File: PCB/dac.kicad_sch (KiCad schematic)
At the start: 29 parts, among them U1 ES9038Q2M, Y1 ASE-50MHz

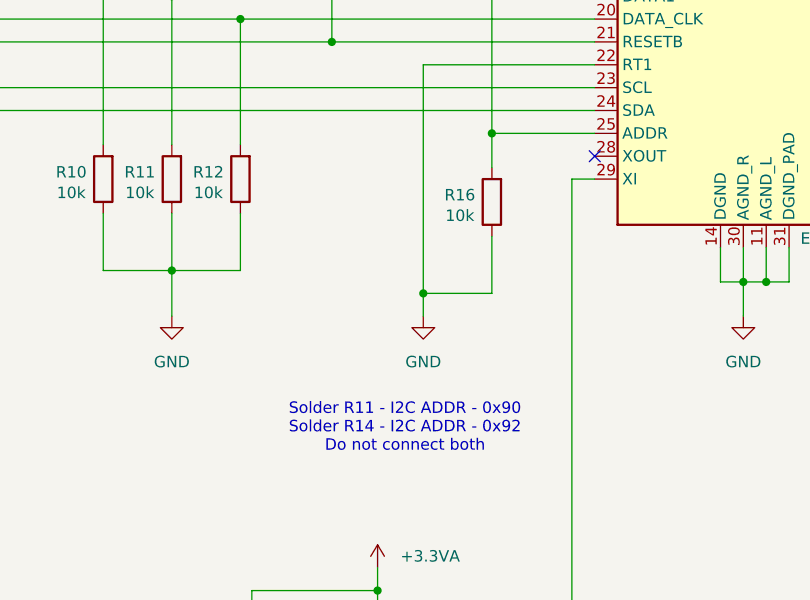
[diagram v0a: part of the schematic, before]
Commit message: Routing revised, added some missing parameters to components
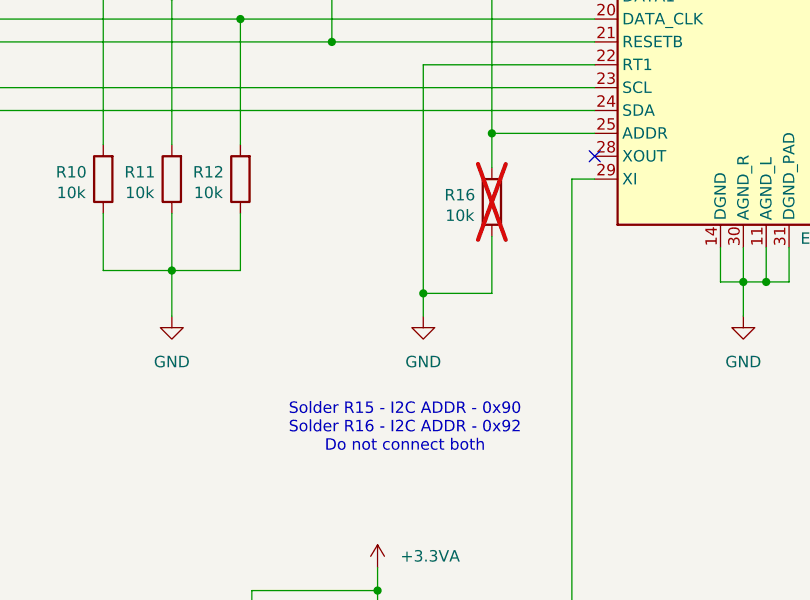
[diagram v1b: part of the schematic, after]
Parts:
- C3, C4, C5, C6, C7, C8: Voltage 6.3V -> 16V
- R16: now not fitted
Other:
- note added: "Solder R15 - I2C ADDR - 0x90 Solder R16 - I2C ADDR - 0x92 Do not connect both"
- note removed: "Solder R11 - I2C ADDR - 0x90 Solder R14 - I2C ADDR - 0x92 Do not connect both"
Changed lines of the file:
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@@
 		)
 	)
-	(text "Solder R11 - I2C ADDR - 0x90\nSolder R14 - I2C ADDR - 0x92\nDo not connect both"
+	(text "Solder R15 - I2C ADDR - 0x90\nSolder R16 - I2C ADDR - 0x92\nDo not connect both"
 		(exclude_from_sim no)
 		(at 135.128 136.906 0)
@@
 			)
 		)
-		(property "Voltage" "6.3V"
+		(property "Voltage" "16V"
 			(at 209.55 33.02 0)
 			(effects
@@
 			)
 		)
-		(property "Voltage" "6.3V"
+		(property "Voltage" "16V"
 			(at 163.83 52.07 0)
 			(effects
@@
 			)
 		)
-		(property "Voltage" "6.3V"
+		(property "Voltage" "16V"
 			(at 220.98 33.02 0)
 			(effects
@@
 		(in_bom yes)
 		(on_board yes)
-		(dnp no)
+		(dnp yes)
 		(property "Reference" "R16"
 			(at 141.224 110.998 0)
@@
 			)
 		)
-		(property "Voltage" "6.3V"
+		(property "Voltage" "16V"
 			(at 243.84 33.02 0)
 			(effects
@@
 			)
 		)
-		(property "Voltage" "6.3V"
+		(property "Voltage" "16V"
 			(at 232.41 33.02 0)
 			(effects
@@
 			)
 		)
-		(property "Voltage" "6.3V"
+		(property "Voltage" "16V"
 			(at 243.84 55.88 0)
 			(effects

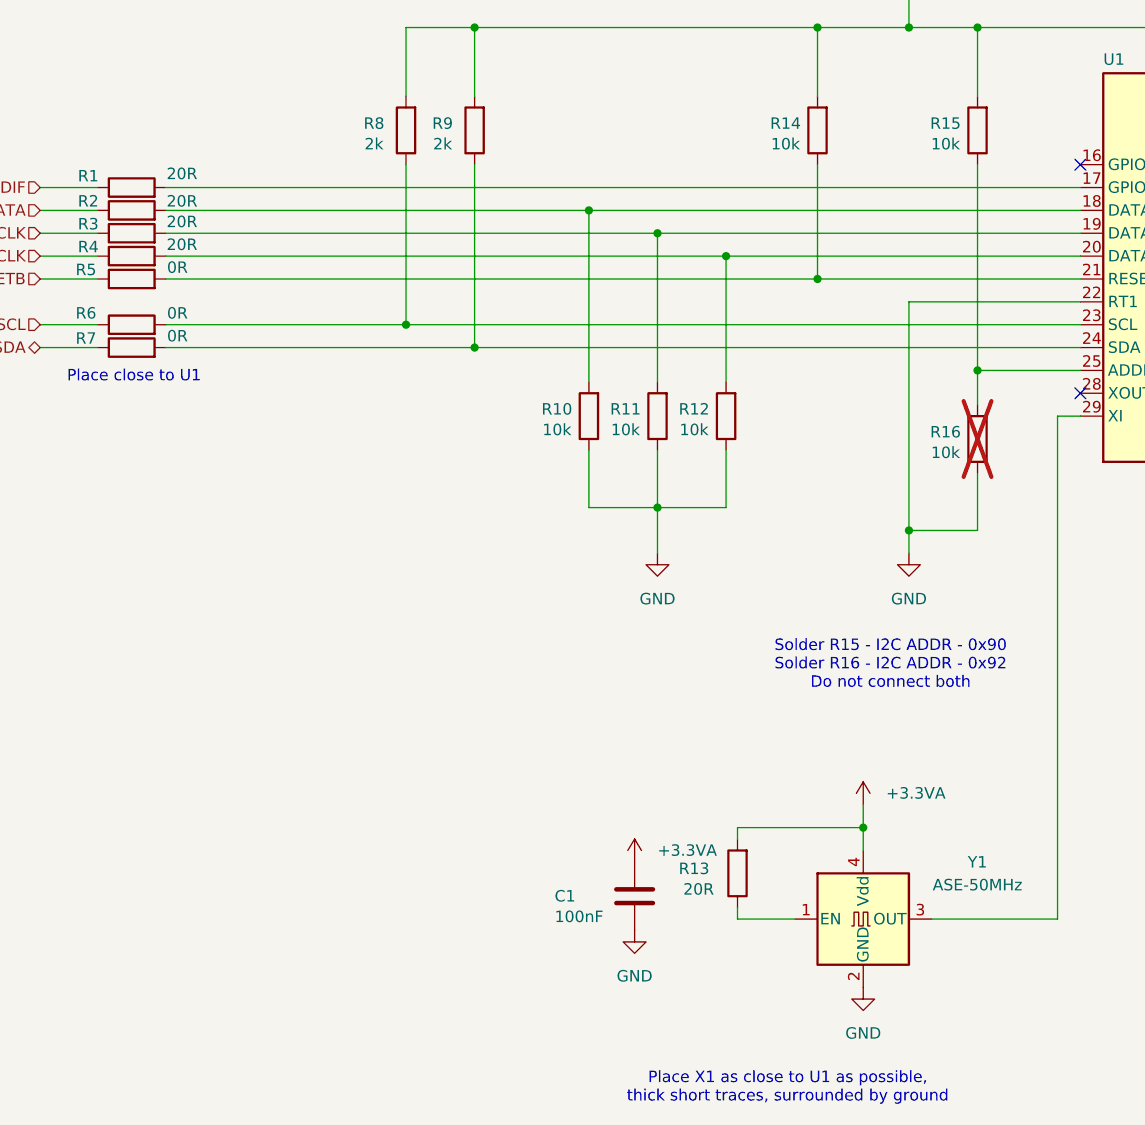
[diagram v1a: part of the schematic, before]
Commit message: Updated PCB with digital traxce suggestions. Added JLCPCB Pns
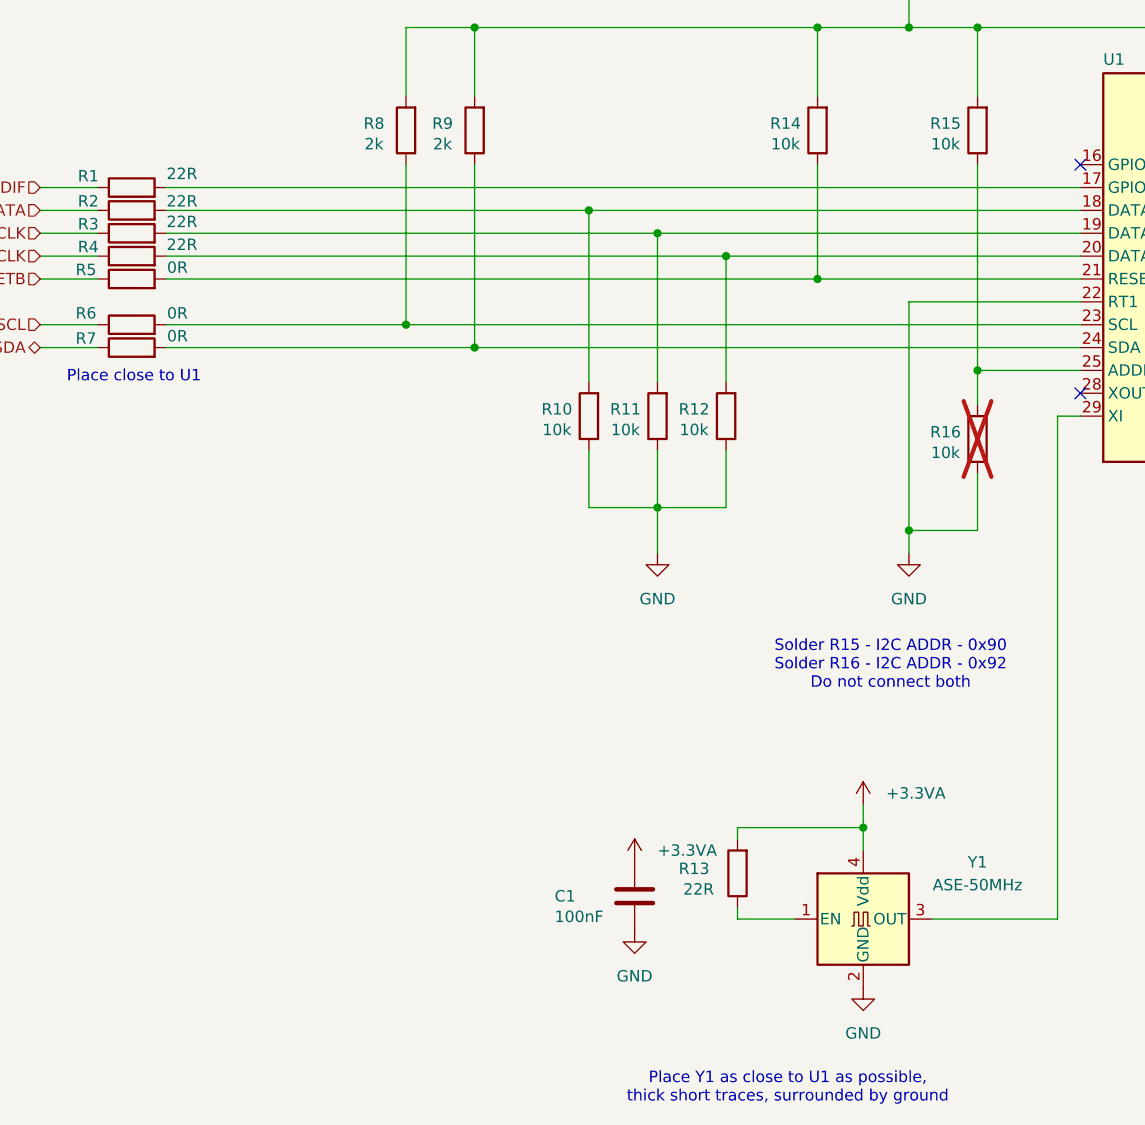
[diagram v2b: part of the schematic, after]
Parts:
- C1: JLCPCBPn (none) -> C1525; Voltage 25V -> 16V
- C3, C4, C5, C6, C7, C8: JLCPCBPn (none) -> C15849
- R1, R13, R2, R3, R4: value 20R -> 22R; JLCPCBPn (none) -> C25092
- R10, R11, R12, R14, R15: JLCPCBPn (none) -> C25744
- R17, R18, R19, R20, R5, R6, R7: JLCPCBPn (none) -> C17168
- R8, R9: JLCPCBPn (none) -> C4109
- U1: JLCPCBPn (none) -> C2682306
- Y1: JLCPCBPn (none) -> C19725350
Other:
- note added: "Place Y1 as close to U1 as possible, thick short traces, surrounded by ground"
- note removed: "Place X1 as close to U1 as possible, thick short traces, surrounded by ground"

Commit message: Added filter capacitors to OPA1622 circuitry
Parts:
- C1: JLCPCBPn C1525 -> (none); LCSC Part # (none) -> C1525
- C3, C4, C5, C6, C7, C8: JLCPCBPn C15849 -> (none); LCSC Part # (none) -> C15849
- R1, R13, R2, R3, R4: JLCPCBPn C25092 -> (none); LCSC Part # (none) -> C25092
- R10, R11, R12, R14, R15: JLCPCBPn C25744 -> (none); LCSC Part # (none) -> C25744
- R17, R18, R19, R20, R5, R6, R7: JLCPCBPn C17168 -> (none); LCSC Part # (none) -> C17168
- R8, R9: JLCPCBPn C4109 -> (none); LCSC Part # (none) -> C4109
- U1: JLCPCBPn C2682306 -> (none); LCSC Part # (none) -> C2682306
- Y1: JLCPCBPn C19725350 -> (none); LCSC Part # (none) -> C19725350
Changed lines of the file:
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@@
 			)
 		)
-		(property "JLCPCBPn" "C4109"
+		(property "LCSC Part #" "C4109"
 			(at 88.9 77.47 0)
 			(effects
@@
 			)
 		)
-		(property "JLCPCBPn" "C15849"
+		(property "LCSC Part #" "C15849"
 			(at 209.55 33.02 0)
 			(effects
@@
 			)
 		)
-		(property "JLCPCBPn" "C25092"
+		(property "LCSC Part #" "C25092"
 			(at 50.8 88.9 0)
 			(effects
@@
 			)
 		)
-		(property "JLCPCBPn" "C1525"
+		(property "LCSC Part #" "C1525"
 			(at 106.68 162.56 0)
 			(effects
@@
 			)
 		)
-		(property "JLCPCBPn" "C15849"
+		(property "LCSC Part #" "C15849"
 			(at 163.83 52.07 0)
 			(effects
@@
 			)
 		)
-		(property "JLCPCBPn" "C15849"
+		(property "LCSC Part #" "C15849"
 			(at 220.98 33.02 0)
 			(effects
@@
 			)
 		)
-		(property "JLCPCBPn" "C25092"
+		(property "LCSC Part #" "C25092"
 			(at 50.8 86.36 0)
 			(effects
@@
 			)
 		)
-		(property "JLCPCBPn" "C25092"
+		(property "LCSC Part #" "C25092"
 			(at 50.8 83.82 0)
 			(effects
@@
 			)
 		)
-		(property "JLCPCBPn" "C25092"
+		(property "LCSC Part #" "C25092"
 			(at 50.8 91.44 0)
 			(effects
@@
 			)
 		)
-		(property "JLCPCBPn" "C19725350"
+		(property "LCSC Part #" "C19725350"
 			(at 132.08 165.1 0)
 			(effects
@@
 			)
 		)
-		(property "JLCPCBPn" "C25744"
+		(property "LCSC Part #" "C25744"
 			(at 116.84 109.22 0)
 			(effects
@@
 			)
 		)
-		(property "JLCPCBPn" "C2682306"
+		(property "LCSC Part #" "C2682306"
 			(at 173.99 92.71 0)
 			(effects
@@
 			)
 		)
-		(property "JLCPCBPn" "C17168"
+		(property "LCSC Part #" "C17168"
 			(at 224.79 101.6 0)
 			(effects
@@
 			)
 		)
-		(property "JLCPCBPn" "C17168"
+		(property "LCSC Part #" "C17168"
 			(at 224.79 83.82 0)
 			(effects
@@
 			)
 		)
-		(property "JLCPCBPn" "C17168"
+		(property "LCSC Part #" "C17168"
 			(at 50.8 93.98 0)
 			(effects
@@
 			)
 		)
-		(property "JLCPCBPn" "C17168"
+		(property "LCSC Part #" "C17168"
 			(at 50.8 101.6 0)
 			(effects
@@
 			)
 		)
-		(property "JLCPCBPn" "C25744"
+		(property "LCSC Part #" "C25744"
 			(at 144.78 77.47 0)
 			(effects
@@
 			)
 		)
-		(property "JLCPCBPn" "C17168"
+		(property "LCSC Part #" "C17168"
 			(at 50.8 99.06 0)
 			(effects
@@
 			)
 		)
-		(property "JLCPCBPn" "C15849"
+		(property "LCSC Part #" "C15849"
 			(at 243.84 33.02 0)
 			(effects
@@
 			)
 		)
-		(property "JLCPCBPn" "C25092"
+		(property "LCSC Part #" "C25092"
 			(at 118.11 160.02 0)
 			(effects
@@
 			)
 		)
-		(property "JLCPCBPn" "C25744"
+		(property "LCSC Part #" "C25744"
 			(at 101.6 109.22 0)
 			(effects
@@
 			)
 		)
-		(property "JLCPCBPn" "C4109"
+		(property "LCSC Part #" "C4109"
 			(at 81.28 77.47 0)
 			(effects
@@
 			)
 		)
-		(property "JLCPCBPn" "C25744"
+		(property "LCSC Part #" "C25744"
 			(at 127 77.47 0)
 			(effects
@@
 			)
 		)
-		(property "JLCPCBPn" "C15849"
+		(property "LCSC Part #" "C15849"
 			(at 232.41 33.02 0)
 			(effects
@@
 			)
 		)
-		(property "JLCPCBPn" "C15849"
+		(property "LCSC Part #" "C15849"
 			(at 243.84 55.88 0)
 			(effects
@@
 			)
 		)
-		(property "JLCPCBPn" "C25744"
+		(property "LCSC Part #" "C25744"
 			(at 109.22 109.22 0)
 			(effects
@@
 			)
 		)
-		(property "JLCPCBPn" "C17168"
+		(property "LCSC Part #" "C17168"
 			(at 224.79 99.06 0)
 			(effects
@@
 			)
 		)
-		(property "JLCPCBPn" "C17168"
+		(property "LCSC Part #" "C17168"
 			(at 224.79 86.36 0)
 			(effects

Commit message: Changed the BOM field for JLCPCB to the original name instead of LCSC
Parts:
- C1: JLCPCB Part # (none) -> C1525; LCSC Part # C1525 -> (none)
- C3, C4, C5, C6, C7, C8: JLCPCB Part # (none) -> C15849; LCSC Part # C15849 -> (none)
- R1, R13, R2, R3, R4: JLCPCB Part # (none) -> C25092; LCSC Part # C25092 -> (none)
- R10, R11, R12, R14, R15: JLCPCB Part # (none) -> C25744; LCSC Part # C25744 -> (none)
- R17, R18, R19, R20, R5, R6, R7: JLCPCB Part # (none) -> C17168; LCSC Part # C17168 -> (none)
- R8, R9: JLCPCB Part # (none) -> C4109; LCSC Part # C4109 -> (none)
- U1: JLCPCB Part # (none) -> C2682306; LCSC Part # C2682306 -> (none)
- Y1: JLCPCB Part # (none) -> C19725350; LCSC Part # C19725350 -> (none)
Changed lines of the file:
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@@
 			)
 		)
-		(property "LCSC Part #" "C4109"
+		(property "JLCPCB Part #" "C4109"
 			(at 88.9 77.47 0)
 			(effects
@@
 			)
 		)
-		(property "LCSC Part #" "C15849"
+		(property "JLCPCB Part #" "C15849"
 			(at 209.55 33.02 0)
 			(effects
@@
 			)
 		)
-		(property "LCSC Part #" "C25092"
+		(property "JLCPCB Part #" "C25092"
 			(at 50.8 88.9 0)
 			(effects
@@
 			)
 		)
-		(property "LCSC Part #" "C1525"
+		(property "JLCPCB Part #" "C1525"
 			(at 106.68 162.56 0)
 			(effects
@@
 			)
 		)
-		(property "LCSC Part #" "C15849"
+		(property "JLCPCB Part #" "C15849"
 			(at 163.83 52.07 0)
 			(effects
@@
 			)
 		)
-		(property "LCSC Part #" "C15849"
+		(property "JLCPCB Part #" "C15849"
 			(at 220.98 33.02 0)
 			(effects
@@
 			)
 		)
-		(property "LCSC Part #" "C25092"
+		(property "JLCPCB Part #" "C25092"
 			(at 50.8 86.36 0)
 			(effects
@@
 			)
 		)
-		(property "LCSC Part #" "C25092"
+		(property "JLCPCB Part #" "C25092"
 			(at 50.8 83.82 0)
 			(effects
@@
 			)
 		)
-		(property "LCSC Part #" "C25092"
+		(property "JLCPCB Part #" "C25092"
 			(at 50.8 91.44 0)
 			(effects
@@
 			)
 		)
-		(property "LCSC Part #" "C19725350"
+		(property "JLCPCB Part #" "C19725350"
 			(at 132.08 165.1 0)
 			(effects
@@
 			)
 		)
-		(property "LCSC Part #" "C25744"
+		(property "JLCPCB Part #" "C25744"
 			(at 116.84 109.22 0)
 			(effects
@@
 			)
 		)
-		(property "LCSC Part #" "C2682306"
+		(property "JLCPCB Part #" "C2682306"
 			(at 173.99 92.71 0)
 			(effects
@@
 			)
 		)
-		(property "LCSC Part #" "C17168"
+		(property "JLCPCB Part #" "C17168"
 			(at 224.79 101.6 0)
 			(effects
@@
 			)
 		)
-		(property "LCSC Part #" "C17168"
+		(property "JLCPCB Part #" "C17168"
 			(at 224.79 83.82 0)
 			(effects
@@
 			)
 		)
-		(property "LCSC Part #" "C17168"
+		(property "JLCPCB Part #" "C17168"
 			(at 50.8 93.98 0)
 			(effects
@@
 			)
 		)
-		(property "LCSC Part #" "C17168"
+		(property "JLCPCB Part #" "C17168"
 			(at 50.8 101.6 0)
 			(effects
@@
 			)
 		)
-		(property "LCSC Part #" "C25744"
+		(property "JLCPCB Part #" "C25744"
 			(at 144.78 77.47 0)
 			(effects
@@
 			)
 		)
-		(property "LCSC Part #" "C17168"
+		(property "JLCPCB Part #" "C17168"
 			(at 50.8 99.06 0)
 			(effects
@@
 			)
 		)
-		(property "LCSC Part #" "C15849"
+		(property "JLCPCB Part #" "C15849"
 			(at 243.84 33.02 0)
 			(effects
@@
 			)
 		)
-		(property "LCSC Part #" "C25092"
+		(property "JLCPCB Part #" "C25092"
 			(at 118.11 160.02 0)
 			(effects
@@
 			)
 		)
-		(property "LCSC Part #" "C25744"
+		(property "JLCPCB Part #" "C25744"
 			(at 101.6 109.22 0)
 			(effects
@@
 			)
 		)
-		(property "LCSC Part #" "C4109"
+		(property "JLCPCB Part #" "C4109"
 			(at 81.28 77.47 0)
 			(effects
@@
 			)
 		)
-		(property "LCSC Part #" "C25744"
+		(property "JLCPCB Part #" "C25744"
 			(at 127 77.47 0)
 			(effects
@@
 			)
 		)
-		(property "LCSC Part #" "C15849"
+		(property "JLCPCB Part #" "C15849"
 			(at 232.41 33.02 0)
 			(effects
@@
 			)
 		)
-		(property "LCSC Part #" "C15849"
+		(property "JLCPCB Part #" "C15849"
 			(at 243.84 55.88 0)
 			(effects
@@
 			)
 		)
-		(property "LCSC Part #" "C25744"
+		(property "JLCPCB Part #" "C25744"
 			(at 109.22 109.22 0)
 			(effects
@@
 			)
 		)
-		(property "LCSC Part #" "C17168"
+		(property "JLCPCB Part #" "C17168"
 			(at 224.79 99.06 0)
 			(effects
@@
 			)
 		)
-		(property "LCSC Part #" "C17168"
+		(property "JLCPCB Part #" "C17168"
 			(at 224.79 86.36 0)
 			(effects

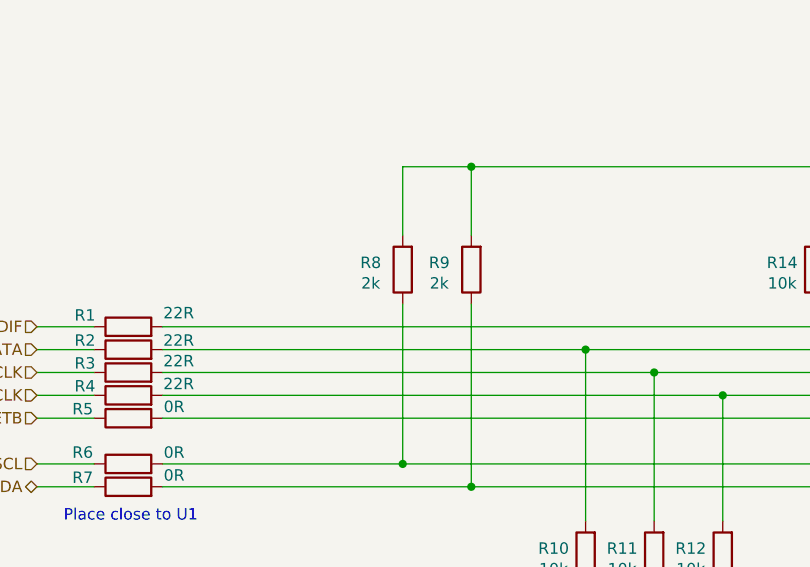
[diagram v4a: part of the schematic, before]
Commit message: Changes in E2P for better identification of the board
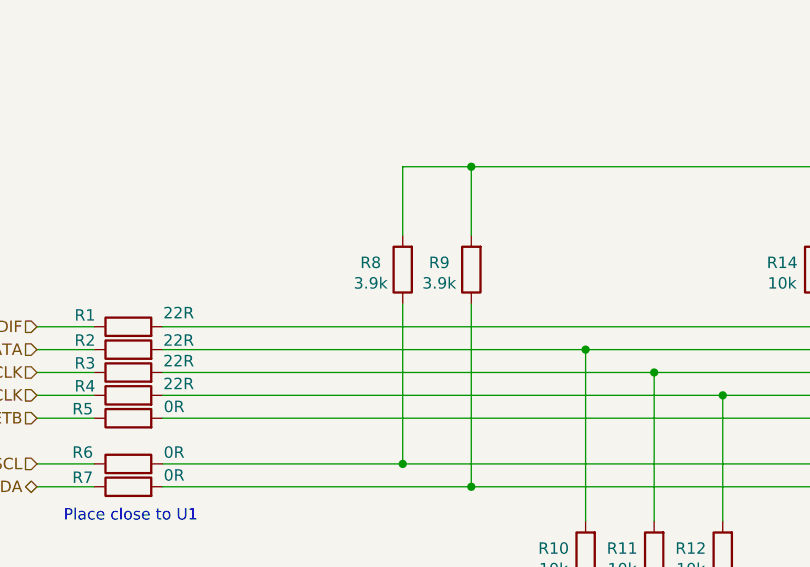
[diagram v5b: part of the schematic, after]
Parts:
- R8, R9: value 2k -> 3.9k; JLCPCB Part # C4109 -> C51721
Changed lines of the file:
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@@
 			)
 		)
-		(property "Value" "2k"
+		(property "Value" "3.9k"
 			(at 85.344 78.994 0)
 			(effects
@@
 			)
 		)
-		(property "JLCPCB Part #" "C4109"
+		(property "JLCPCB Part #" "C51721"
 			(at 88.9 77.47 0)
 			(effects
@@
 			)
 		)
-		(property "Value" "2k"
+		(property "Value" "3.9k"
 			(at 77.724 78.994 0)
 			(effects
@@
 			)
 		)
-		(property "JLCPCB Part #" "C4109"
+		(property "JLCPCB Part #" "C51721"
 			(at 81.28 77.47 0)
 			(effects
